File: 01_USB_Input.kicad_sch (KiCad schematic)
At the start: 10 parts, among them J1 USB_C_Receptacle_USB2.0_16P, U3 USBLC6-2SC6

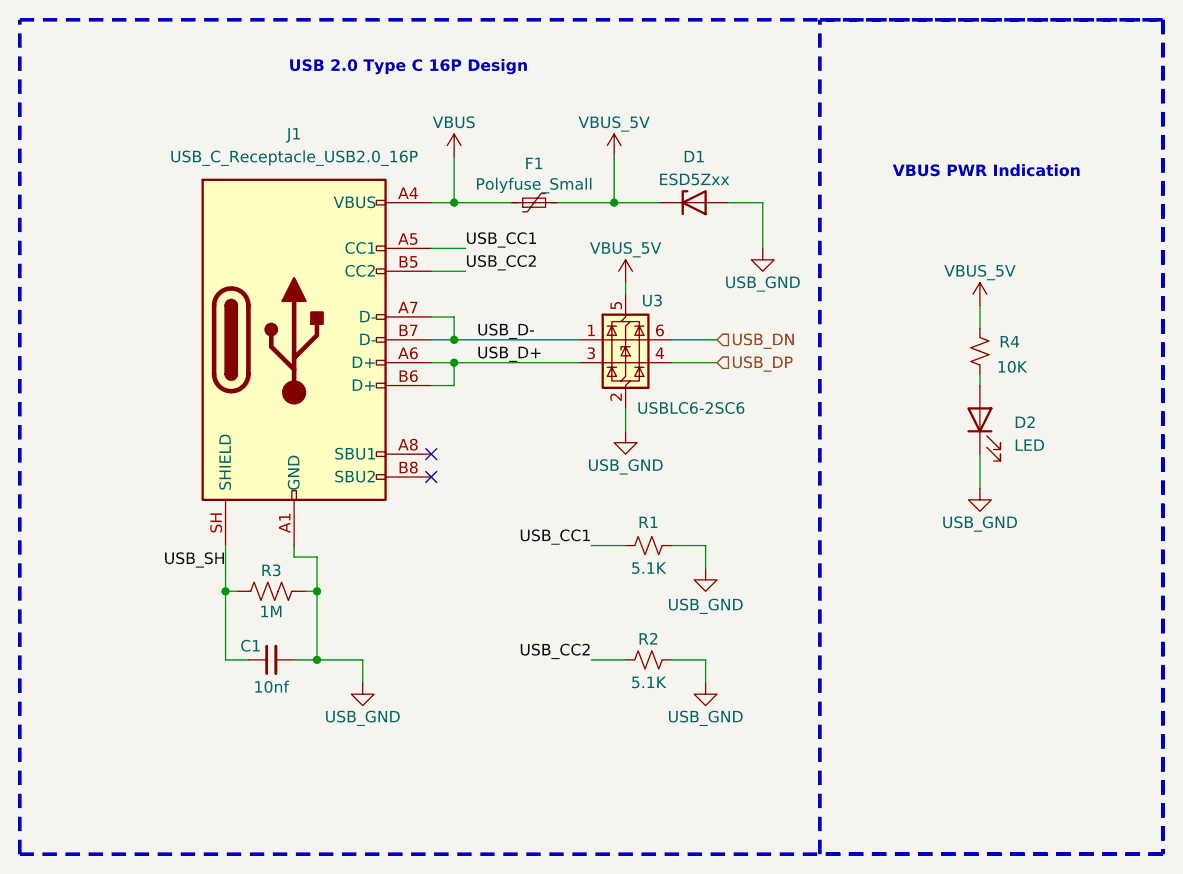
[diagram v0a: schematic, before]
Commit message: completed schematic design, and selected all footprints and for now will go for 0805 for resistors, capacitors and leds - will later make a call during layoting
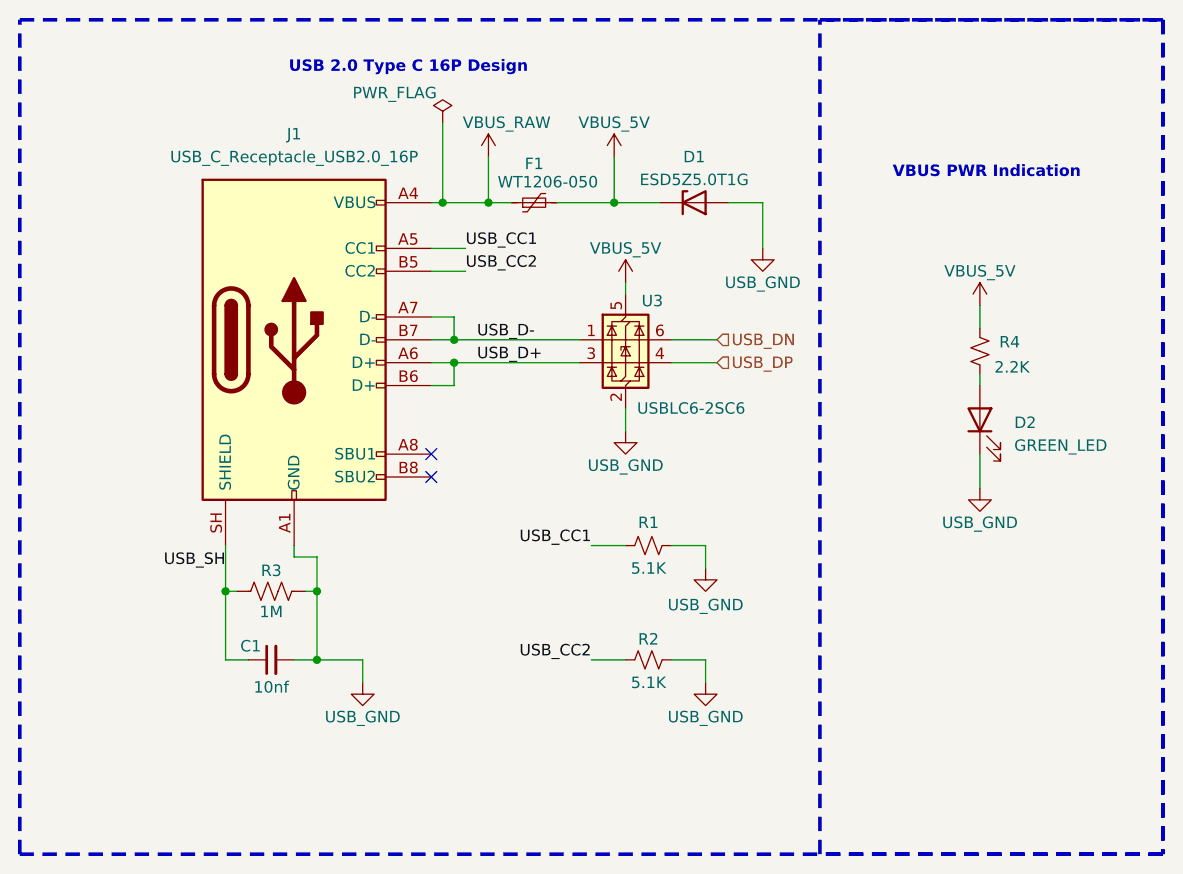
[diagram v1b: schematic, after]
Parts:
- D1: value ESD5Zxx -> ESD5Z5.0T1G; Link (none) -> https://www.lioncircuits.com/parts/ESD5Z5.0T1G?srsltid=AfmB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
- D2: value LED -> GREEN_LED
- F1: value Polyfuse_Small -> WT1206-050; footprint (none) -> Fuse:Fuse_1206_3216Metric_Pad1.42x1.75mm_HandSolder; Link (none) -> https://sharvielectronics.com/product/wt1206-050-pptc-reset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
- R4: value 10K -> 2.2K
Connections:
- net VBUS renamed VBUS_RAW
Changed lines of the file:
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@@
 	)
 	(junction
-		(at 137.16 67.31)
+		(at 140.97 67.31)
+		(diameter 0)
+		(color 0 0 0 0)
+	)
+	(junction
+		(at 135.89 67.31)
 		(diameter 0)
 		(color 0 0 0 0)
@@
 	(wire
 		(pts
+			(xy 135.89 67.31) (xy 140.97 67.31)
+		)
+		(stroke
+			(width 0)
+			(type default)
+		)
+	)
+	(wire
+		(pts
 			(xy 120.65 110.49) (xy 121.92 110.49)
 		)
@@
 	(wire
 		(pts
+			(xy 135.89 58.42) (xy 135.89 67.31)
+		)
+		(stroke
+			(width 0)
+			(type default)
+		)
+	)
+	(wire
+		(pts
 			(xy 113.03 110.49) (xy 111.76 110.49)
 		)
@@
 	(wire
 		(pts
-			(xy 137.16 67.31) (xy 143.51 67.31)
-		)
-		(stroke
-			(width 0)
-			(type default)
-		)
-	)
-	(wire
-		(pts
 			(xy 137.16 80.01) (xy 137.16 82.55)
 		)
@@
 	(wire
 		(pts
+			(xy 140.97 67.31) (xy 143.51 67.31)
+		)
+		(stroke
+			(width 0)
+			(type default)
+		)
+	)
+	(wire
+		(pts
 			(xy 121.92 110.49) (xy 121.92 118.11)
 		)
@@
 	(wire
 		(pts
-			(xy 137.16 62.23) (xy 137.16 67.31)
+			(xy 140.97 62.23) (xy 140.97 67.31)
 		)
 		(stroke
@@
 	(wire
 		(pts
-			(xy 134.62 67.31) (xy 137.16 67.31)
+			(xy 134.62 67.31) (xy 135.89 67.31)
 		)
 		(stroke
@@
 				(path "/b7bfdaa0-038f-4b80-877f-94c6e9c4db2c/f34af6bf-b008-49a2-8565-d5eee961a5ed"
 					(reference "R1")
+					(unit 1)
+				)
+			)
+		)
+	)
+	(symbol
+		(lib_id "power:PWR_FLAG")
+		(at 135.89 58.42 0)
+		(unit 1)
+		(body_style 1)
+		(exclude_from_sim no)
+		(in_bom yes)
+		(on_board yes)
+		(in_pos_files yes)
+		(dnp no)
+		(property "Reference" "#FLG01"
+			(at 135.89 56.515 0)
+			(hide yes)
+			(show_name no)
+			(do_not_autoplace no)
+			(effects
+				(font
+					(size 1.27 1.27)
+				)
+			)
+		)
+		(property "Value" "PWR_FLAG"
+			(at 130.556 55.118 0)
+			(show_name no)
+			(do_not_autoplace no)
+			(effects
+				(font
+					(size 1.27 1.27)
+				)
+			)
+		)
+		(property "Footprint" ""
+			(at 135.89 58.42 0)
+			(hide yes)
+			(show_name no)
+			(do_not_autoplace no)
+			(effects
+				(font
+					(size 1.27 1.27)
+				)
+			)
+		)
+		(property "Datasheet" ""
+			(at 135.89 58.42 0)
+			(hide yes)
+			(show_name no)
+			(do_not_autoplace no)
+			(effects
+				(font
+					(size 1.27 1.27)
+				)
+			)
+		)
+		(property "Description" "Special symbol for telling ERC where power comes from"
+			(at 135.89 58.42 0)
+			(hide yes)
+			(show_name no)
+			(do_not_autoplace no)
+			(effects
+				(font
+					(size 1.27 1.27)
+				)
+			)
+		)
+		(pin "1"
+		)
+		(instances
+			(project "HWE-Isolated-USB-to-UART-Design"
+				(path "/b7bfdaa0-038f-4b80-877f-94c6e9c4db2c/f34af6bf-b008-49a2-8565-d5eee961a5ed"
+					(reference "#FLG01")
 					(unit 1)
 				)
@@
 			)
 		)
-		(property "Value" "10K"
+		(property "Value" "2.2K"
 			(at 199.136 85.598 0)
 			(show_name no)
@@
 			)
 		)
-		(property "Value" "Polyfuse_Small"
-			(at 146.05 65.278 90)
-			(show_name no)
-			(do_not_autoplace no)
-			(effects
-				(font
-					(size 1.27 1.27)
-				)
-			)
-		)
-		(property "Footprint" ""
+		(property "Value" "WT1206-050"
+			(at 147.574 65.024 90)
+			(show_name no)
+			(do_not_autoplace no)
+			(effects
+				(font
+					(size 1.27 1.27)
+				)
+			)
+		)
+		(property "Footprint" "Fuse:Fuse_1206_3216Metric_Pad1.42x1.75mm_HandSolder"
 			(at 151.13 66.04 0)
 			(hide yes)
@@
 		(property "Description" "Resettable fuse, polymeric positive temperature coefficient, small symbol"
 			(at 146.05 67.31 0)
+			(hide yes)
+			(show_name no)
+			(do_not_autoplace no)
+			(effects
+				(font
+					(size 1.27 1.27)
+				)
+			)
+		)
+		(property "Link" "https://sharvielectronics.com/product/wt1206-050-pptc-resettable-fuse-fuse-6v-500ma-1206-package/?srsltid=AfmBOooZ-QqrnW0wS0_e6LutVeNZSuHTBTzuZISC6iU85kQOpFlGASu-"
+			(at 146.05 67.31 90)
 			(hide yes)
 			(show_name no)
@@
 			)
 		)
-		(property "Value" "ESD5Zxx"
+		(property "Value" "ESD5Z5.0T1G"
 			(at 163.83 64.77 0)
 			(show_name no)
@@
 		)
 		(property "Description" "ESD Protection Diode, SOD-523"
+			(at 163.83 67.31 0)
+			(hide yes)
+			(show_name no)
+			(do_not_autoplace no)
+			(effects
+				(font
+					(size 1.27 1.27)
+				)
+			)
+		)
+		(property "Link" "https://www.lioncircuits.com/parts/ESD5Z5.0T1G?srsltid=AfmBOop8Hnb_ssgq6vq52z1SgommCiPQPrxm-6Xce4t_LaQ80rv-LdHY"
 			(at 163.83 67.31 0)
 			(hide yes)
@@
 	(symbol
 		(lib_id "PCM_SparkFun-PowerSymbol:VBUS")
-		(at 137.16 62.23 0)
+		(at 140.97 62.23 0)
 		(unit 1)
 		(body_style 1)
@@
 		(in_pos_files yes)
 		(dnp no)
-		(fields_autoplaced yes)
 		(property "Reference" "#PWR07"
-			(at 137.16 66.04 0)
-			(hide yes)
-			(show_name no)
-			(do_not_autoplace no)
-			(effects
-				(font
-					(size 1.27 1.27)
-				)
-			)
-		)
-		(property "Value" "VBUS"
-			(at 137.16 58.42 0)
+			(at 140.97 66.04 0)
+			(hide yes)
+			(show_name no)
+			(do_not_autoplace no)
+			(effects
+				(font
+					(size 1.27 1.27)
+				)
+			)
+		)
+		(property "Value" "VBUS_RAW"
+			(at 143.002 58.42 0)
 			(show_name no)
 			(do_not_autoplace yes)
@@
 		)
 		(property "Footprint" ""
-			(at 137.16 62.23 0)
+			(at 140.97 62.23 0)
 			(hide yes)
 			(show_name no)
@@
 		)
 		(property "Datasheet" ""
-			(at 137.16 62.23 0)
+			(at 140.97 62.23 0)
 			(hide yes)
 			(show_name no)
@@
 		)
 		(property "Description" "Power symbol creates a global label with name \"VBUS\""
-			(at 137.16 68.58 0)
+			(at 140.97 68.58 0)
 			(hide yes)
 			(show_name no)
@@
 			)
 		)
-		(property "Value" "LED"
+		(property "Value" "GREEN_LED"
 			(at 199.39 94.2974 90)
 			(show_name no)
